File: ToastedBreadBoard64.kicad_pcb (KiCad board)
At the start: 2 copper layers, 55.9 x 95.2 mm, 9 parts, among them J1 Conn_02x20_Odd_Even, J2 Conn_02x20_Odd_Even, J4 Conn_02x20_Odd_Even, J5 Conn_02x20_Odd_Even, U1 DIL126

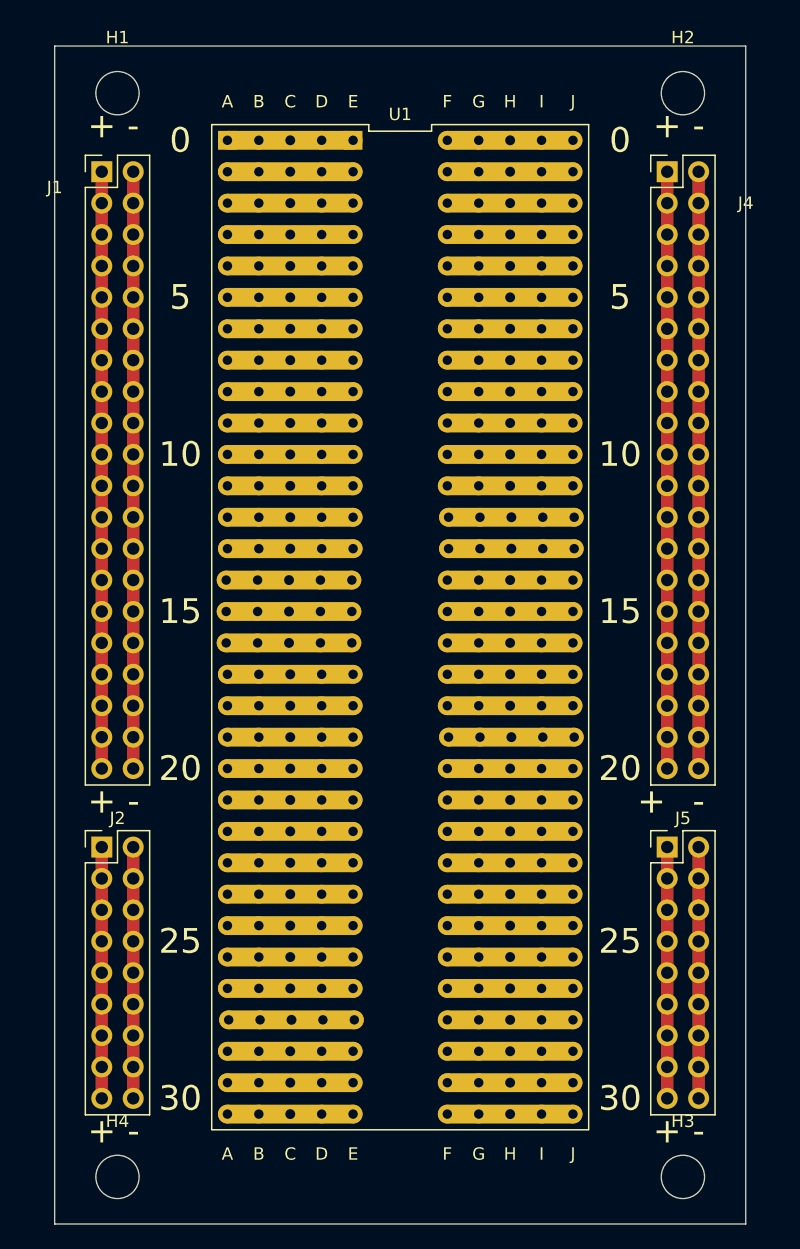
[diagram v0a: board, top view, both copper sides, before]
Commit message: Make all holes the same size.
Signed-off-by: John Bradley <flypie@rocketmail.com>
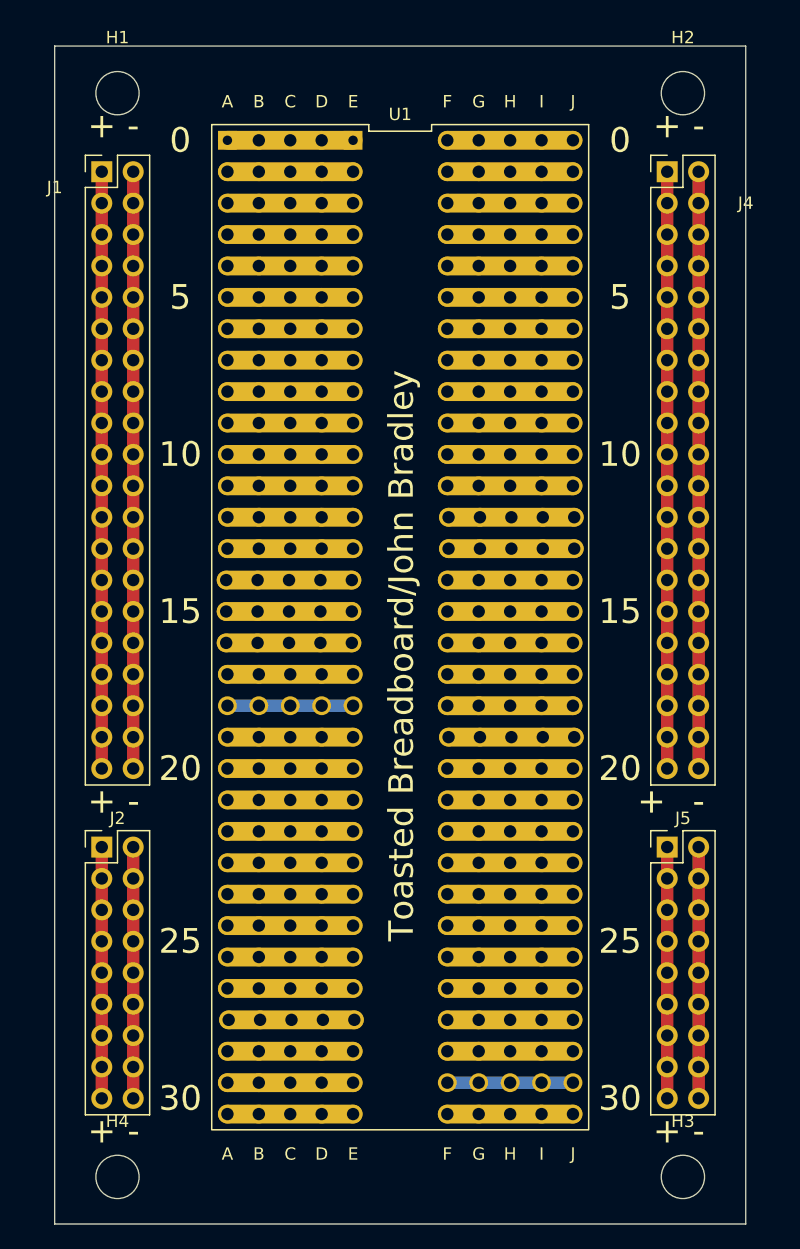
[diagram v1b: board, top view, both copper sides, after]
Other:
- board text added: "Toasted Breadboard/John Bradley"

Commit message: Correct width.
Signed-off-by: John Bradley <flypie@rocketmail.com>
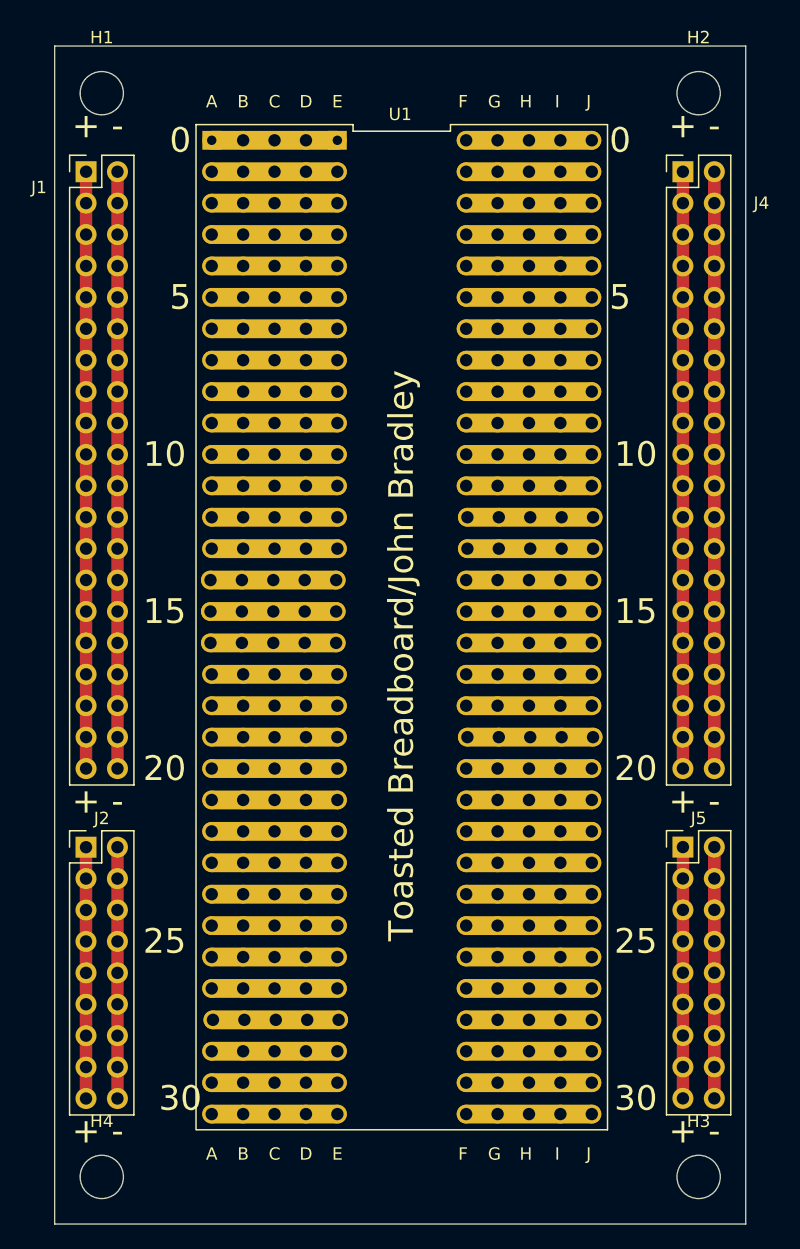
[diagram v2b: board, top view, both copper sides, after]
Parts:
- moved J2 1.28 mm to (104.1, 85.1)
- moved H1 1.27 mm to (105.4, 24.1)
- moved H4 1.27 mm to (105.4, 111.8)
- moved J4 1.27 mm to (152.4, 30.5)
- moved J5 1.27 mm to (152.4, 85.1)
- moved J1 1.27 mm to (104.1, 30.5)
- moved H2 1.27 mm to (153.7, 24.1)
- moved H3 1.27 mm to (153.7, 111.8)
